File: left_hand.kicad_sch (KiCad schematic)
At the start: 1 part

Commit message: Design power
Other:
- title: Port Plover -> Stenoswitch
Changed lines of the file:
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@@
 	(paper "A5")
 	(title_block
-		(title "Port Plover")
-		(date "2025-07-28")
+		(title "Stenoswitch")
 		(rev "0.1")
 		(company "https://github.com/Bennett-Petzold/port_plover")

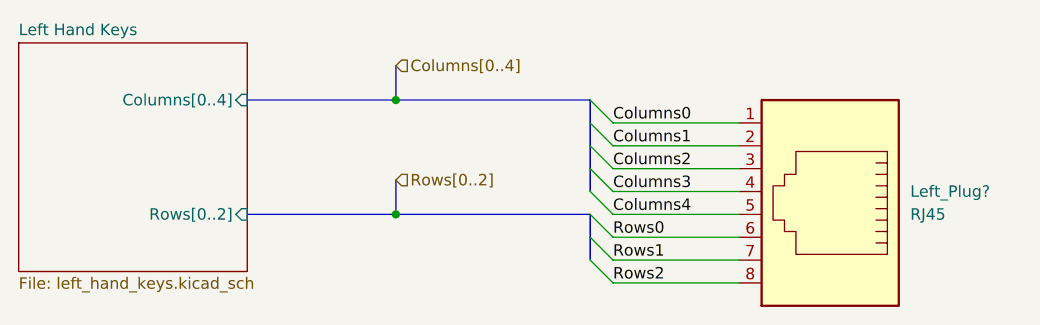
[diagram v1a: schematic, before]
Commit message: Rework battery entirely
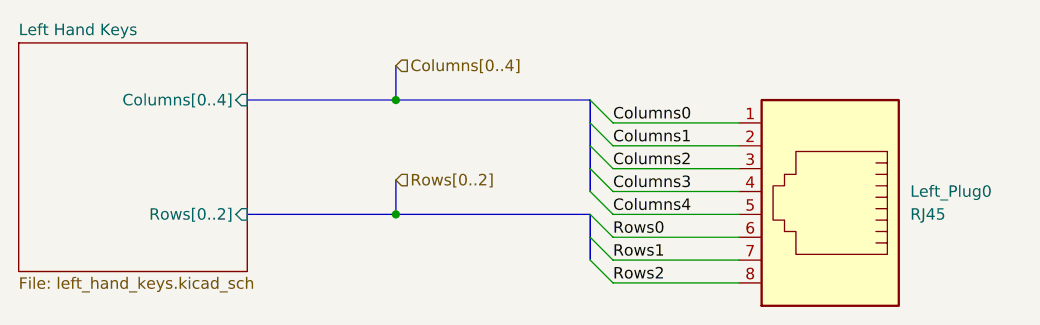
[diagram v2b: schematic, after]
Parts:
- Left_Plug0: renamed from Left_Plug?; footprint (none) -> custom:942
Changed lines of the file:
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@@
 		(dnp no)
 		(fields_autoplaced yes)
-		(property "Reference" "Left_Plug?"
+		(property "Reference" "Left_Plug0"
 			(at 157.48 64.7699 0)
 			(effects
@@
 			)
 		)
-		(property "Footprint" ""
+		(property "Footprint" "custom:942"
 			(at 148.59 65.405 90)
 			(effects
@@
 			(project "portable_steno"
 				(path "/06a6eca0-edda-4cc0-a23f-017602e67f07/2477db2d-d681-4372-a745-e817369fb274"
-					(reference "Left_Plug?")
+					(reference "Left_Plug0")
 					(unit 1)
 				)

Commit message: Assign footprints
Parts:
- Left_Plug0: footprint custom:942 -> custom:8P8C_942
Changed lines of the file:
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@@
 			)
 		)
-		(property "Footprint" "custom:942"
+		(property "Footprint" "custom:8P8C_942"
 			(at 148.59 65.405 90)
 			(effects

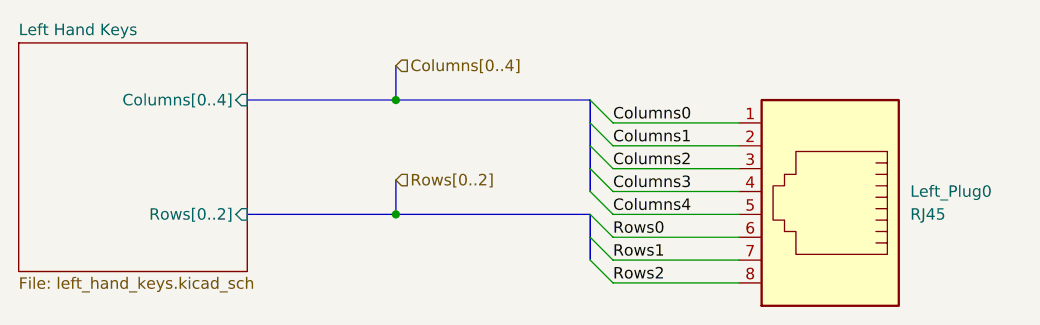
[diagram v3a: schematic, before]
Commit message: Init right and left PCBs
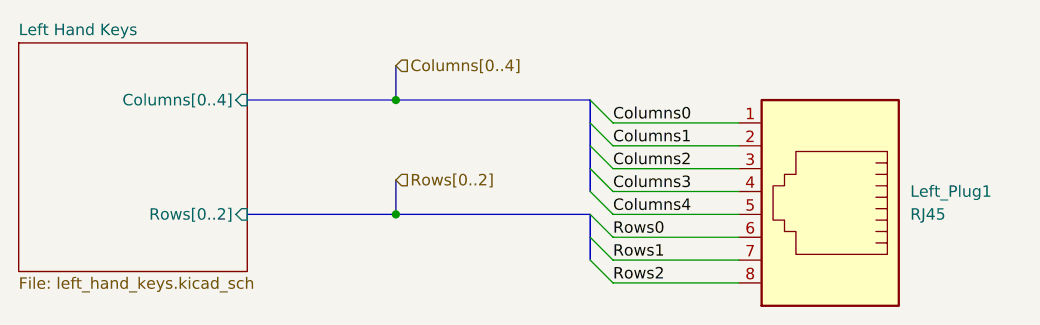
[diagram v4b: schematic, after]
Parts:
- renumbered Left_Plug0 to Left_Plug1
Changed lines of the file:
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@@
 		(dnp no)
 		(fields_autoplaced yes)
-		(property "Reference" "Left_Plug0"
+		(property "Reference" "Left_Plug1"
 			(at 157.48 64.7699 0)
 			(effects
@@
 				)
 			)
+			(project "left_hand"
+				(path "/efcccfe8-5e20-4b1b-8d3b-61fce771481e"
+					(reference "Left_Plug1")
+					(unit 1)
+				)
+			)
 		)
 	)
@@
 				)
 			)
+			(project "left_hand"
+				(path "/efcccfe8-5e20-4b1b-8d3b-61fce771481e"
+					(page "2")
+				)
+			)
 		)
 	)
+	(sheet_instances
+		(path "/"
+			(page "1")
+		)
+	)
+	(embedded_fonts no)
 )

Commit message: Layout left hand side
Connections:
- net Columns0: now also Left_Plug1.2; no longer Left_Plug1.1
- net Columns1: now also Left_Plug1.3; no longer Left_Plug1.2
- net Columns2: now also Left_Plug1.4; no longer Left_Plug1.3
- net Columns3: now also Left_Plug1.1; no longer Left_Plug1.4
- net Rows0: now also Left_Plug1.7; no longer Left_Plug1.6
- net Rows1: now also Left_Plug1.6; no longer Left_Plug1.7
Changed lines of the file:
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@@
 		)
 	)
-	(label "Columns0"
+	(label "Columns3"
 		(at 124.46 57.15 0)
 		(effects
@@
 		)
 	)
-	(label "Columns1"
+	(label "Columns0"
 		(at 124.46 59.69 0)
 		(effects
@@
 		)
 	)
-	(label "Columns3"
+	(label "Columns2"
 		(at 124.46 64.77 0)
 		(effects
@@
 		)
 	)
-	(label "Columns2"
+	(label "Columns1"
 		(at 124.46 62.23 0)
 		(effects
@@
 		)
 	)
-	(label "Rows0"
+	(label "Rows1"
 		(at 124.46 69.85 0)
 		(effects
@@
 		)
 	)
-	(label "Rows1"
+	(label "Rows0"
 		(at 124.46 72.39 0)
 		(effects
